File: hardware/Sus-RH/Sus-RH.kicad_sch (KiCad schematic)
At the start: 40 parts, among them J1 MX150_02x06_Vertical, J2 53307-2471, J4 Conn_01x06, J5 Conn_01x06, U1 TLV9002QDRQ1, U2 LDO40LPURY

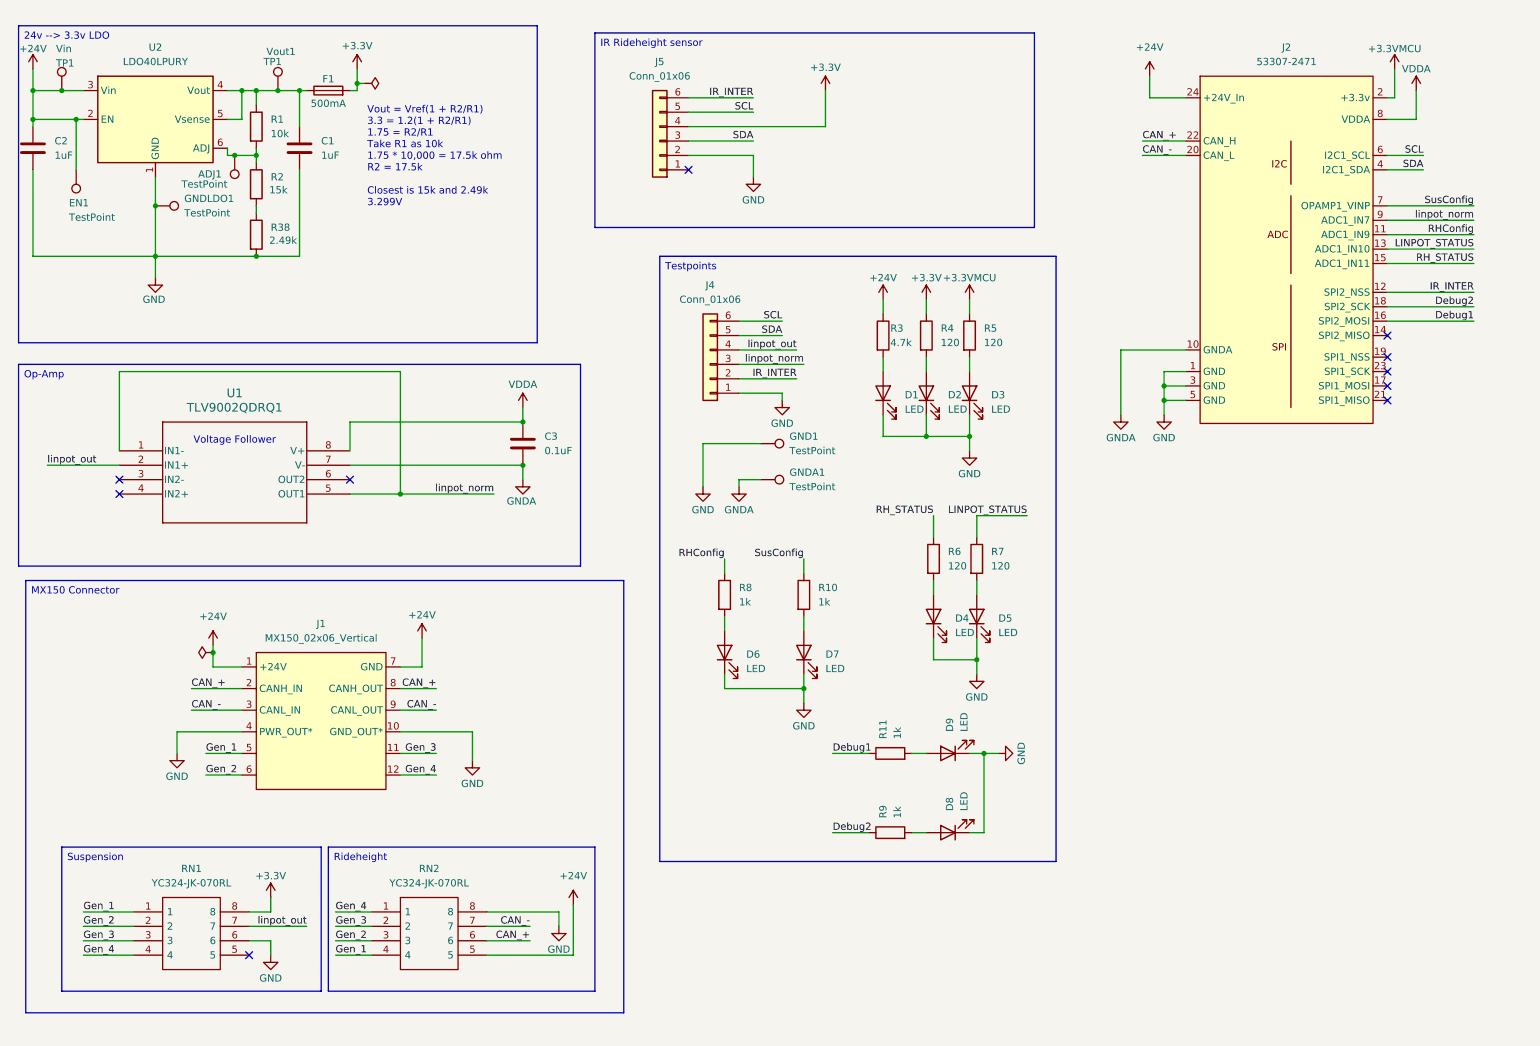
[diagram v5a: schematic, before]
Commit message: Rev B Review (#2)
* schematic changes: ldo switched out of qfn, op amp footprint fixed, resistor array changed. need add correct stm changes

* finished sch + removed LDO

* removed LDO, added correct cube.

* op-amp changes

* layout finished, need to add some more silkscreen + ready for review!

* finished layout + silkscreen, ready to review.

* mac files removed

* made changes from review council

* added 3d models for 01x05 nanofits

* added stepfiles for sus-rh

* sus-rh production ready

* remove .DS_Store files

* fixed nanofit for linpot

* added "validated silkscreen"

* Added jlc assembly files

* pitot board sch review. the biggest change was the switch to nanofits and different pressure sensor

---------

Co-authored-by: Lakshay983 <56173382+Lakshay983@users.noreply.github.com>
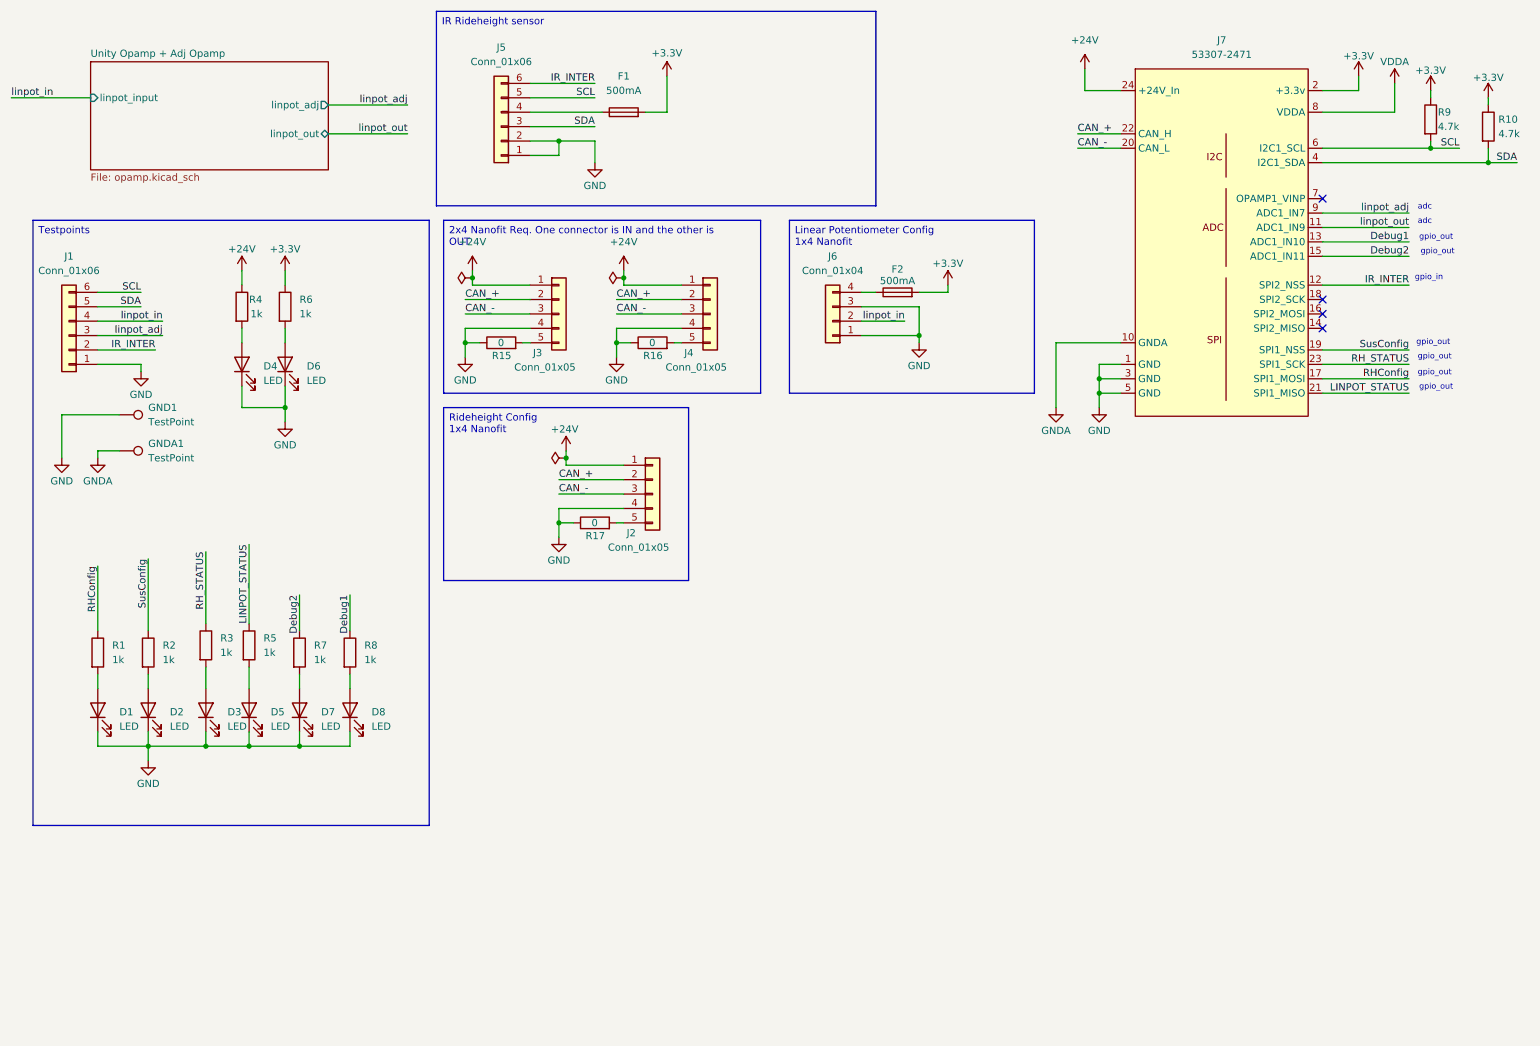
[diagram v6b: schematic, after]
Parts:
- removed ADJ1, EN1, GNDLDO1: TestPoint, TestPoint:TestPoint_Pad_D1.0mm, symbol Connector:TestPoint
- removed C1, C2: 1uF, Capacitor_SMD:C_0603_1608Metric_Pad1.08x0.95mm_HandSolder, symbol Device:C
- removed C3: 0.1uF, Capacitor_SMD:C_0603_1608Metric_Pad1.08x0.95mm_HandSolder, symbol Device:C
- removed D3: LED, LED_SMD:LED_0603_1608Metric_Pad1.05x0.95mm_HandSolder, symbol Device:LED
- removed J1: MX150_02x06_Vertical, UTSVT_Connectors:MX150_02x06_Vertical, symbol utsvt_connectors:MX150_02x06_Vertical
- removed R1: 10k, Resistor_SMD:R_0603_1608Metric_Pad0.98x0.95mm_HandSolder, symbol Device:R
- removed R2: 15k, Resistor_SMD:R_0603_1608Metric_Pad0.98x0.95mm_HandSolder, symbol Device:R
- removed R38: 2.49k, Resistor_SMD:R_0603_1608Metric_Pad0.98x0.95mm_HandSolder, symbol Device:R
- removed R5: 120, Resistor_SMD:R_0603_1608Metric_Pad0.98x0.95mm_HandSolder, symbol Device:R
- removed RN1, RN2: YC324-JK-070RL, 4pinRes:YC324JK07220RL, symbol YC324-JK-070RL:YC324-JK-070RL
- removed U1: TLV9002QDRQ1, footprints:SOIC8_D_TEX, symbol TLV9002QDRQ1:TLV9002QDRQ1
- removed U2: LDO40LPURY, Package_DFN_QFN:DFN-6-1EP_3x3mm_P0.95mm_EP1.7x2.6mm, symbol Regulator_Linear:LDO40LPURY
- removed Vin, Vout1: TP1, TestPoint:TestPoint_Pad_D1.0mm, symbol Connector:TestPoint
- added F2: 500mA, Fuse:Fuse_0603_1608Metric_Pad1.05x0.95mm_HandSolder, symbol Device:Fuse
- added J2, J3, J4: Conn_01x05, Connector_Molex:Molex_Nano-Fit_105313-xx05_1x05_P2.50mm_Horizontal, symbol Connector_Generic:Conn_01x05
- added J6: Conn_01x04, Connector_Molex:Molex_Nano-Fit_105313-xx04_1x04_P2.50mm_Horizontal, symbol Connector_Generic:Conn_01x04
- added R10, R9: 4.7k, Resistor_SMD:R_0603_1608Metric_Pad0.98x0.95mm_HandSolder, symbol Device:R
- added R15, R16, R17: 0, Resistor_SMD:R_0603_1608Metric_Pad0.98x0.95mm_HandSolder, symbol Device:R
- F1: footprint Fuse:Fuseholder_Blade_Mini_Keystone_3568 -> Fuse:Fuse_0603_1608Metric_Pad1.05x0.95mm_HandSolder; P/N 3568 -> 0603L050YR
- GND1: footprint TestPoint:TestPoint_Pad_1.0x1.0mm -> TestPoint:TestPoint_THTPad_2.5x2.5mm_Drill1.2mm
- GNDA1: footprint TestPoint:TestPoint_Pad_1.0x1.0mm -> TestPoint:TestPoint_THTPad_1.5x1.5mm_Drill0.7mm
- R3: renamed from R6; value 120 -> 1k
- R4: renamed from R3; value 4.7k -> 1k
- R5: renamed from R7; value 120 -> 1k
- R6: renamed from R4; value 120 -> 1k
- renumbered D6 to D1, D7 to D2, D4 to D3, D1 to D4, D2 to D6, D8 to D7, D9 to D8, J4 to J1, J2 to J7, R8 to R1, R10 to R2, R9 to R7, R11 to R8
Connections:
- net +3.3VMCU is gone; now on net +3.3V: J7.2 (+3.3v)
- net +24V: now also J2.1 (Pin_1), J3.1 (Pin_1), J4.1 (Pin_1)
- net +3.3V: now also F2.2, R10.1, R9.1; no longer J5.4 (Pin_4)
- net CAN_+: now also J2.2 (Pin_2), J3.2 (Pin_2), J4.2 (Pin_2)
- net CAN_-: now also J2.3 (Pin_3), J3.3 (Pin_3), J4.3 (Pin_3)
- net Debug1: now also J7.13 (ADC1_IN10); no longer J7.16 (SPI2_MOSI)
- net Debug2: now also J7.15 (ADC1_IN11); no longer J7.18 (SPI2_SCK)
- net GND: now also J5.1 (Pin_1), J2.4 (Pin_4), J3.4 (Pin_4), J4.4 (Pin_4), J6.1 (Pin_1), J6.3 (Pin_3), R15.1, R16.1, R17.1
- net LINPOT_STATUS: now also J7.21 (SPI1_MISO); no longer J7.13 (ADC1_IN10)
- net RHConfig: now also J7.17 (SPI1_MOSI); no longer J7.11 (ADC1_IN9)
- net RH_STATUS: now also J7.23 (SPI1_SCK); no longer J7.15 (ADC1_IN11)
- net SCL: now also R9.2
- net SDA: now also R10.2
- net SusConfig: now also J7.19 (SPI1_NSS); no longer J7.7 (OPAMP1_VINP)
- net linpot_out: now also J7.11 (ADC1_IN9); no longer J1.4 (Pin_4)
- net at F1.1: now also J5.4 (Pin_4)
- net linpot_norm renamed linpot_adj
- new net: J3.5 (Pin_5), R15.2
- new net: J2.5 (Pin_5), R17.2
- new net: J4.5 (Pin_5), R16.2
- new net: F2.1, J6.4 (Pin_4)
- new net linpot_in: J1.4 (Pin_4), J6.2 (Pin_2)
- no-connect marks 10 -> 4
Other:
- added sheet Unity Opamp + Adj Opamp (opamp.kicad_sch)
- note added: "adc"
- note added: "gpio_in"
- note added: "gpio_out"
- note removed: "Voltage Follower"
- note removed: "Vout = Vref(1 + R2/R1) 3.3 = 1.2(1 + R2/R1) 1.75 = R2/R1 Take R1 as 10k 1.75 * 10,000 = 17.5k ohm R2 = 17.5k Closest is 15k and 2.49k 3.299V"
- moved on the sheet: D1, D2, D3, D4, D5, D6, D7, D8, GND1, GNDA1, J1, J5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

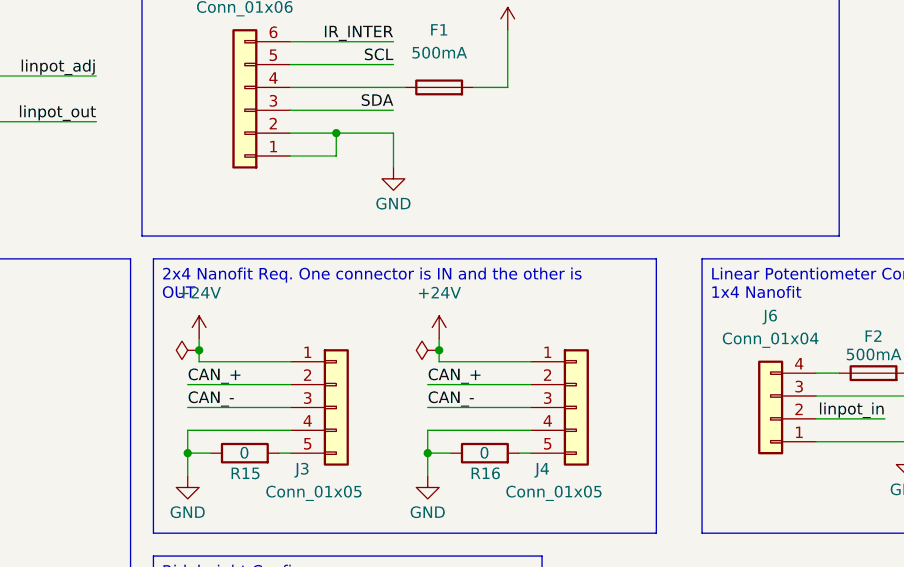
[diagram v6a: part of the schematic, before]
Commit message: Pitot Board Rev B (#3)
* init

* added layout

* ready to review

* finished pitot board

* pitot board ordered, routing+size finished for temperature board so pull??

* finished tempboard silkscreen

* resized temperature board

* poo oo ee

* ughhhhhhhhhhhhhhhhhhghghghhhhhhhhhhhhhhhhhhh

* working i2c on RH board

* cleanup?

* small

* added read me

* fixed mistake

* Fix image filename case in README.md

* Add new line for telemetry components explanation
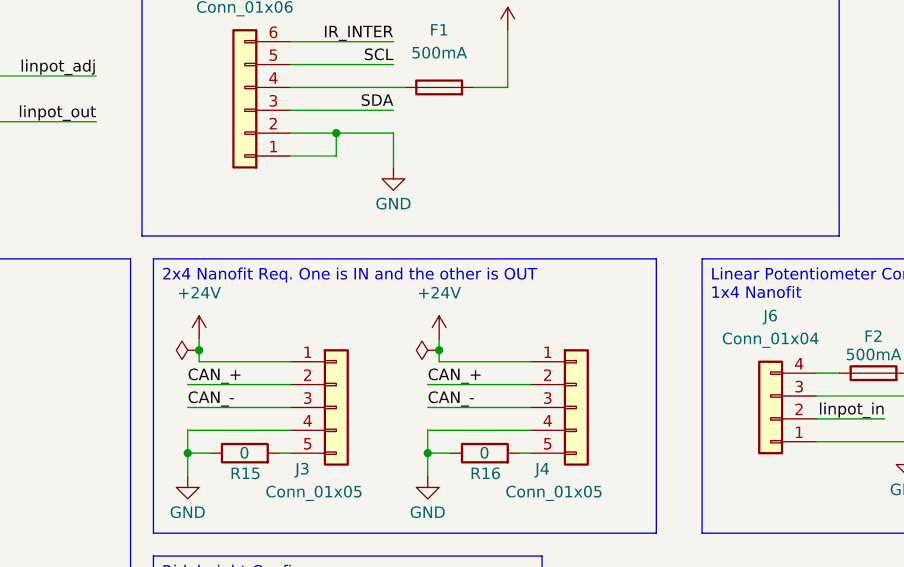
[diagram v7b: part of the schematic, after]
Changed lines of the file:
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@@
 		)
 	)
-	(text_box "2x4 Nanofit Req. One connector is IN and the other is OUT"
+	(text_box "2x4 Nanofit Req. One is IN and the other is OUT"
 		(exclude_from_sim no)
 		(at 91.44 50.8 0)

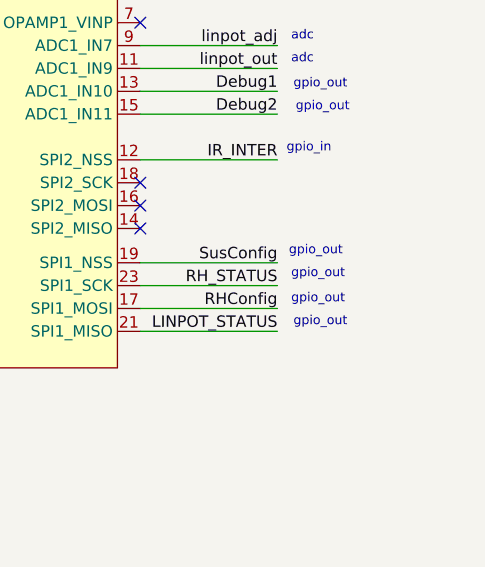
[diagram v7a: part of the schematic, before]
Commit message: datapacking, working interrupts, and CAN Transmit working on linpots
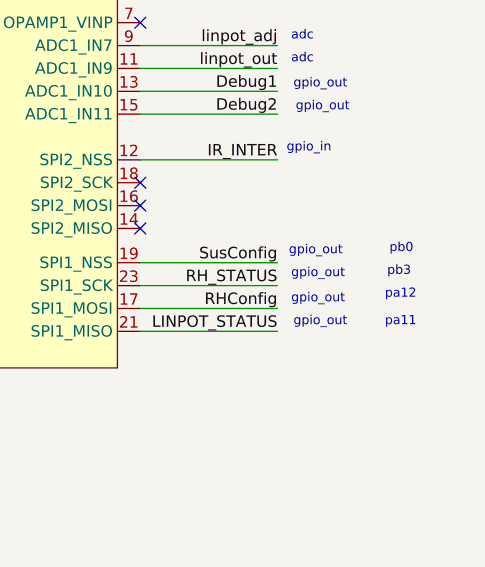
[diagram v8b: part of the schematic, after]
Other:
- note added: "pa11"
- note added: "pa12"
- note added: "pb0"
- note added: "pb3"
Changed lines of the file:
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@@
+		)
+	)
+	(text "pb0"
+		(exclude_from_sim no)
+		(at 274.066 72.136 0)
+		(effects
+			(font
+				(size 1.016 1.016)
+			)
+			(justify left)
+		)
+	)
+	(text "pb3\n"
+		(exclude_from_sim no)
+		(at 273.812 74.676 0)
+		(effects
+			(font
+				(size 1.016 1.016)
+			)
+			(justify left)
+		)
+	)
+	(text "pa11"
+		(exclude_from_sim no)
+		(at 273.558 80.264 0)
+		(effects
+			(font
+				(size 1.016 1.016)
+			)
+			(justify left)
 		)
 	)
@@
 		(effects
 			(font
+				(size 1.016 1.016)
+			)
+			(justify left)
+		)
+	)
+	(text "pa12\n"
+		(exclude_from_sim no)
+		(at 273.558 77.216 0)
+		(effects
+			(font
